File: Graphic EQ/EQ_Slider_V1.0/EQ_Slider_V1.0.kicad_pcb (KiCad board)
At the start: 2 copper layers, 101.6 x 63.5 mm, 27 parts

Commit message: small updates
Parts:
- moved TP1 3.23 mm to (195.8, 85.0)
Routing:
- net Net-(RV1-Pad3): track 148.7 -> 151.9 mm
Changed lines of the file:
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@@
 			(psa4output no)
 			(plot_black_and_white yes)
-			(plotinvisibletext no)
 			(sketchpadsonfab no)
 			(plotpadnumbers no)
@@
 	(footprint "HiroFootprints:Out_Hole_3.4_1.8"
 		(layer "F.Cu")
-		(at 195.8 88.23)
+		(at 195.8 85)
 		(property "Reference" "TP1"
 			(at 0 -0.5 0)
@@
 		)
 		(property "Value" "Cut (L)"
-			(at 0 -2.855875 0)
+			(at 0 3 0)
 			(unlocked yes)
 			(layer "F.SilkS")
@@
 	)
 	(segment
-		(start 195.8 88.23)
-		(end 195.8 122.39)
-		(width 1.6)
-		(layer "F.Cu")
-		(net 15)
-	)
-	(segment
 		(start 142.02 124.77)
 		(end 144 126.75)
@@
 		(width 1.6)
 		(layer "F.Cu")
+		(net 15)
+	)
+	(segment
+		(start 195.8 122.39)
+		(end 195.8 85)
+		(width 1.6)
+		(layer "F.Cu")

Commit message: Made slider board more compact
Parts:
- moved TP1 19.8 mm to (195.9, 104.8)
- moved TP3 19.8 mm to (195.9, 90.7)
- moved TP2 19.8 mm to (195.9, 98.1)
- moved REF** 6.27 mm to (196.6, 126.4)
- moved REF** 6.27 mm to (196.6, 71.5)
- moved REF** 0.40 mm to (109.9, 126.4)
- moved REF** 0.39 mm to (109.9, 71.5)
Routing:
- net Net-(RV1-Pad3): track 151.9 -> 128.0 mm
- net Net-(RV1-Pad1): track 69.2 -> 84.6 mm
- net Net-(C1-Pad1): track 92.2 -> 106.9 mm
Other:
- board size 101.6 x 63.5 mm -> 95.3 x 63.5 mm
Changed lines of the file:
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@@
 	(footprint "MountingHole:MountingHole_4mm"
 		(layer "F.Cu")
-		(at 202.82 126.03)
+		(at 196.56 126.43)
 		(descr "Mounting Hole 4mm, no annular")
 		(tags "mounting hole 4mm no annular")
@@
 	(footprint "HiroFootprints:Out_Hole_3.4_1.8"
 		(layer "F.Cu")
-		(at 195.8 85)
+		(at 195.88 104.84)
 		(property "Reference" "TP1"
 			(at 0 -0.5 0)
@@
 	(footprint "MountingHole:MountingHole_4mm"
 		(layer "F.Cu")
-		(at 109.82 71.15)
+		(at 109.88 71.54)
 		(descr "Mounting Hole 4mm, no annular")
 		(tags "mounting hole 4mm no annular")
@@
 	(footprint "HiroFootprints:Out_Hole_3.4_1.8"
 		(layer "F.Cu")
-		(at 195.8 70.83)
+		(at 195.88 90.67)
 		(property "Reference" "TP3"
 			(at 0 -0.5 0)
@@
 	(footprint "MountingHole:MountingHole_4mm"
 		(layer "F.Cu")
-		(at 202.82 71.15)
+		(at 196.56 71.54)
 		(descr "Mounting Hole 4mm, no annular")
 		(tags "mounting hole 4mm no annular")
@@
 	(footprint "MountingHole:MountingHole_4mm"
 		(layer "F.Cu")
-		(at 109.82 126.03)
+		(at 109.88 126.43)
 		(descr "Mounting Hole 4mm, no annular")
 		(tags "mounting hole 4mm no annular")
@@
 	(footprint "HiroFootprints:Out_Hole_3.4_1.8"
 		(layer "F.Cu")
-		(at 195.8 78.23)
+		(at 195.88 98.07)
 		(property "Reference" "TP2"
 			(at 0 -0.5 0)
@@
 	)
 	(gr_rect
-		(start 105.52 66.84)
-		(end 207.12 130.34)
+		(start 105.58 67.24)
+		(end 200.83 130.74)
 		(stroke
 			(width 0.05)
@@
 	)
 	(gr_text "Ver 1.0"
-		(at 186.31 101.29 0)
+		(at 184.88 101.36 0)
 		(layer "F.SilkS")
 		(effects
@@
 	)
 	(gr_text "HCF\nEQ Slider"
-		(at 188.62 98.85 0)
+		(at 187.19 98.92 0)
 		(layer "F.SilkS")
 		(effects
@@
 	)
 	(segment
-		(start 195.79 70.82)
-		(end 195.8 70.83)
+		(start 136.33 70.81)
+		(end 147.0975 70.81)
 		(width 1.6)
 		(layer "F.Cu")
@@
 	)
 	(segment
-		(start 136.33 70.81)
-		(end 147.0975 70.81)
+		(start 195.88 79.75)
+		(end 195.88 90.67)
+		(width 1.6)
+		(layer "F.Cu")
+		(net 1)
+	)
+	(segment
+		(start 186.95 70.82)
+		(end 195.88 79.75)
 		(width 1.6)
 		(layer "F.Cu")
@@
 	)
 	(segment
-		(start 147.0975 70.81)
-		(end 162.4475 70.81)
+		(start 177.5875 70.82)
+		(end 186.95 70.82)
 		(width 1.6)
 		(layer "F.Cu")
@@
 	)
 	(segment
-		(start 115.46 82.22)
-		(end 126.87 70.81)
+		(start 147.0975 70.81)
+		(end 162.4475 70.81)
 		(width 1.6)
 		(layer "F.Cu")
@@
 	)
 	(segment
-		(start 177.5875 70.82)
-		(end 195.79 70.82)
+		(start 115.46 82.22)
+		(end 126.87 70.81)
 		(width 1.6)
 		(layer "F.Cu")
@@
 	(segment
 		(start 188.18 118.495)
-		(end 188.18 124.68)
+		(end 188.18 125.88)
 		(width 1.6)
 		(layer "F.Cu")
@@
 	)
 	(segment
-		(start 191.44 126.75)
-		(end 190.25 126.75)
-		(width 1.6)
-		(layer "F.Cu")
-		(net 15)
-	)
-	(segment
-		(start 182.5 126.75)
-		(end 190.25 126.75)
+		(start 126.64 124.89)
+		(end 126.75 125)
 		(width 1.6)
 		(layer "F.Cu")
@@
 	)
 	(segment
-		(start 126.64 124.89)
-		(end 126.75 125)
+		(start 157.41 124.66)
+		(end 159.5 126.75)
 		(width 1.6)
 		(layer "F.Cu")
@@
 	)
 	(segment
-		(start 195.8 122.39)
-		(end 191.44 126.75)
+		(start 157.41 118.495)
+		(end 157.41 124.66)
 		(width 1.6)
 		(layer "F.Cu")
@@
 	)
 	(segment
-		(start 157.41 124.66)
-		(end 159.5 126.75)
+		(start 188.18 125.88)
+		(end 188.185 125.885)
 		(width 1.6)
 		(layer "F.Cu")
@@
 	)
 	(segment
-		(start 157.41 118.495)
-		(end 157.41 124.66)
+		(start 142.02 124.77)
+		(end 144 126.75)
 		(width 1.6)
 		(layer "F.Cu")
@@
 	)
 	(segment
-		(start 142.02 124.77)
-		(end 144 126.75)
+		(start 174.75 126.75)
+		(end 187.32 126.75)
 		(width 1.6)
 		(layer "F.Cu")
@@
 	)
 	(segment
-		(start 188.18 124.68)
-		(end 190.25 126.75)
+		(start 187.32 126.75)
+		(end 188.185 125.885)
 		(width 1.6)
 		(layer "F.Cu")
@@
 	)
 	(segment
-		(start 174.75 126.75)
-		(end 182.5 126.75)
+		(start 142.02 118.495)
+		(end 142.02 124.77)
 		(width 1.6)
 		(layer "F.Cu")
@@
 	)
 	(segment
-		(start 142.02 118.495)
-		(end 142.02 124.77)
+		(start 195.88 118.19)
+		(end 195.88 104.84)
 		(width 1.6)
 		(layer "F.Cu")
@@
 	)
 	(segment
-		(start 195.8 122.39)
-		(end 195.8 85)
+		(start 159.5 126.75)
+		(end 174.75 126.75)
 		(width 1.6)
 		(layer "F.Cu")
@@
 	)
 	(segment
-		(start 159.5 126.75)
-		(end 174.75 126.75)
+		(start 188.185 125.885)
+		(end 195.88 118.19)
 		(width 1.6)
 		(layer "F.Cu")
@@
 	)
 	(segment
-		(start 195.785 78.215)
-		(end 195.8 78.23)
+		(start 172.79 78.215)
+		(end 188.18 78.215)
 		(width 1.6)
 		(layer "F.Cu")
@@
 	)
 	(segment
-		(start 172.79 78.215)
-		(end 188.18 78.215)
+		(start 126.64 78.215)
+		(end 142.02 78.215)
 		(width 1.6)
 		(layer "F.Cu")
@@
 	)
 	(segment
-		(start 126.64 78.215)
-		(end 142.02 78.215)
+		(start 188.18 90.37)
+		(end 195.88 98.07)
 		(width 1.6)
 		(layer "F.Cu")
@@
 	(segment
 		(start 188.18 78.215)
-		(end 195.785 78.215)
+		(end 188.18 90.37)
 		(width 1.6)
 		(layer "F.Cu")
@@
 		)
 	)
+	(group ""
+		(members "0c7bc8e3-a588-43e6-956f-7a970030289d" "d775e616-bb41-4192-8a43-31805b470f2c")
+	)
 	(embedded_fonts no)

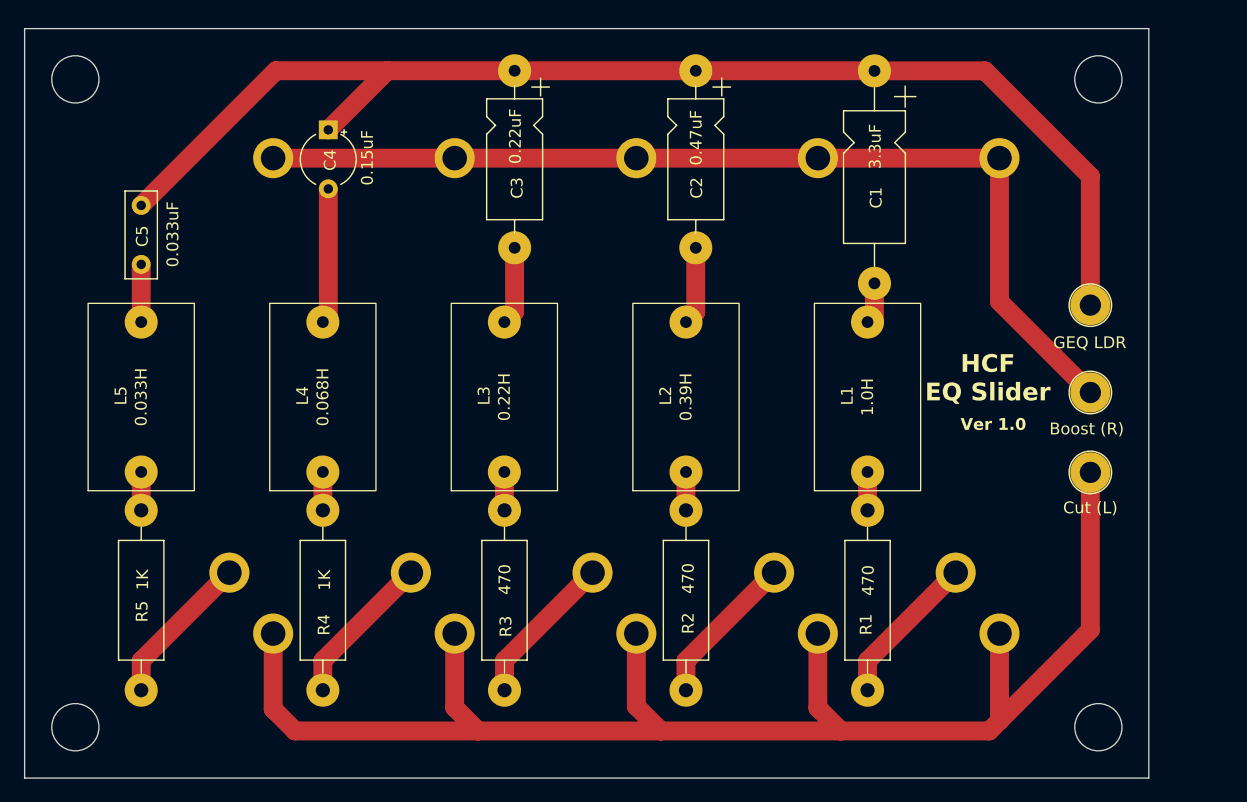
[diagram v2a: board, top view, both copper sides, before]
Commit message: increased trace width
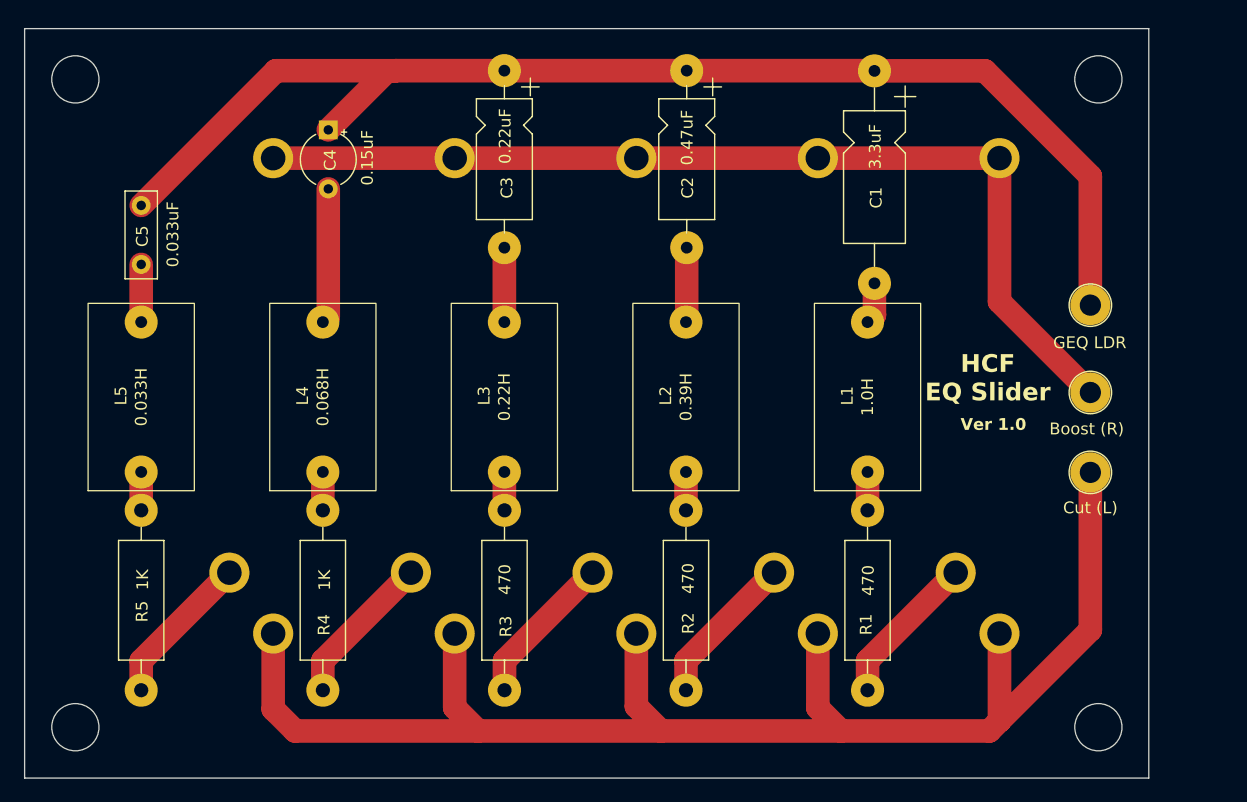
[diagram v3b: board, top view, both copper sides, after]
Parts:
- moved C3 0.87 mm to (146.2, 70.8)
- moved C2 0.77 mm to (161.7, 70.8)
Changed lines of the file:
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@@
 	(footprint "Capacitor_THT:CP_Axial_L10.0mm_D4.5mm_P15.00mm_Horizontal"
 		(layer "F.Cu")
-		(at 162.4475 70.81 -90)
+		(at 161.68 70.8 -90)
 		(descr "CP, Axial series, Axial, Horizontal, pin pitch=15mm, , length*diameter=10*4.5mm^2, Electrolytic Capacitor, , http://www.vishay.com/docs/28325/021asm.pdf")
 		(tags "CP Axial series Axial Horizontal pin pitch 15mm  length 10mm diameter 4.5mm Electrolytic Capacitor")
@@
 	(footprint "Capacitor_THT:CP_Axial_L10.0mm_D4.5mm_P15.00mm_Horizontal"
 		(layer "F.Cu")
-		(at 147.0975 70.81 -90)
+		(at 146.23 70.8 -90)
 		(descr "CP, Axial series, Axial, Horizontal, pin pitch=15mm, , length*diameter=10*4.5mm^2, Electrolytic Capacitor, , http://www.vishay.com/docs/28325/021asm.pdf")
 		(tags "CP Axial series Axial Horizontal pin pitch 15mm  length 10mm diameter 4.5mm Electrolytic Capacitor")
@@
 	)
 	(segment
-		(start 162.4475 70.81)
-		(end 177.5775 70.81)
-		(width 1.6)
-		(layer "F.Cu")
-		(net 1)
-	)
-	(segment
-		(start 136.33 70.81)
-		(end 147.0975 70.81)
-		(width 1.6)
-		(layer "F.Cu")
-		(net 1)
-	)
-	(segment
 		(start 195.88 79.75)
 		(end 195.88 90.67)
-		(width 1.6)
+		(width 2)
 		(layer "F.Cu")
 		(net 1)
@@
 		(start 186.95 70.82)
 		(end 195.88 79.75)
-		(width 1.6)
+		(width 2)
+		(layer "F.Cu")
+		(net 1)
+	)
+	(segment
+		(start 146.23 70.8)
+		(end 161.68 70.8)
+		(width 2)
 		(layer "F.Cu")
 		(net 1)
@@
 		(start 131.31 75.82)
 		(end 136.32 70.81)
-		(width 1.6)
+		(width 2)
 		(layer "F.Cu")
 		(net 1)
@@
 		(start 177.5875 70.82)
 		(end 186.95 70.82)
-		(width 1.6)
+		(width 2)
 		(layer "F.Cu")
 		(net 1)
 	)
 	(segment
-		(start 147.0975 70.81)
-		(end 162.4475 70.81)
-		(width 1.6)
+		(start 161.68 70.8)
+		(end 177.5675 70.8)
+		(width 2)
+		(layer "F.Cu")
+		(net 1)
+	)
+	(segment
+		(start 136.99 70.81)
+		(end 137 70.8)
+		(width 2)
 		(layer "F.Cu")
 		(net 1)
@@
 		(start 115.46 82.22)
 		(end 126.87 70.81)
-		(width 1.6)
+		(width 2)
 		(layer "F.Cu")
 		(net 1)
 	)
 	(segment
-		(start 136.32 70.81)
-		(end 136.33 70.81)
-		(width 1.6)
+		(start 136.33 70.81)
+		(end 136.99 70.81)
+		(width 2)
 		(layer "F.Cu")
 		(net 1)
 	)
 	(segment
-		(start 177.5775 70.81)
+		(start 177.5675 70.8)
 		(end 177.5875 70.82)
-		(width 1.6)
+		(width 2)
+		(layer "F.Cu")
+		(net 1)
+	)
+	(segment
+		(start 137 70.8)
+		(end 146.23 70.8)
+		(width 2)
+		(layer "F.Cu")
+		(net 1)
+	)
+	(segment
+		(start 136.32 70.81)
+		(end 136.33 70.81)
+		(width 2)
 		(layer "F.Cu")
 		(net 1)
@@
 		(start 126.87 70.81)
 		(end 136.33 70.81)
-		(width 1.6)
+		(width 2)
 		(layer "F.Cu")
 		(net 1)
@@
 		(start 177.5875 88.82)
 		(end 177.5875 91.5175)
-		(width 1.6)
+		(width 2)
 		(layer "F.Cu")
 		(net 2)
@@
 		(start 177.5875 91.5175)
 		(end 177 92.105)
-		(width 1.6)
+		(width 2)
 		(layer "F.Cu")
 		(net 2)
 	)
 	(segment
-		(start 162.4475 85.81)
-		(end 162.4475 91.275)
-		(width 1.6)
+		(start 161.68 92.0425)
+		(end 161.6175 92.105)
+		(width 2)
 		(layer "F.Cu")
 		(net 3)
 	)
 	(segment
-		(start 162.4475 91.275)
-		(end 161.6175 92.105)
-		(width 1.6)
+		(start 161.68 85.8)
+		(end 161.68 92.0425)
+		(width 2)
 		(layer "F.Cu")
 		(net 3)
 	)
 	(segment
-		(start 147.0975 91.2375)
+		(start 146.23 85.8)
 		(end 146.23 92.105)
-		(width 1.6)
-		(layer "F.Cu")
-		(net 4)
-	)
-	(segment
-		(start 147.0975 85.81)
-		(end 147.0975 91.2375)
-		(width 1.6)
+		(width 2)
 		(layer "F.Cu")
 		(net 4)
@@
 		(start 177 123.295)
 		(end 177 120.805)
-		(width 1.6)
+		(width 2)
 		(layer "F.Cu")
 		(net 5)
@@
 		(start 177 120.805)
 		(end 184.47 113.335)
-		(width 1.6)
+		(width 2)
 		(layer "F.Cu")
 		(net 5)
@@
 		(start 177 104.805)
 		(end 177 108.055)
-		(width 1.6)
+		(width 2)
 		(layer "F.Cu")
 		(net 6)
@@
 		(start 161.6175 104.805)
 		(end 161.6175 108.055)
-		(width 1.6)
+		(width 2)
 		(layer "F.Cu")
 		(net 7)
@@
 		(start 161.6175 120.7975)
 		(end 169.08 113.335)
-		(width 1.6)
+		(width 2)
 		(layer "F.Cu")
 		(net 8)
@@
 		(start 161.6175 123.295)
 		(end 161.6175 120.7975)
-		(width 1.6)
+		(width 2)
 		(layer "F.Cu")
 		(net 8)
@@
 		(start 146.24 120.795)
 		(end 153.7 113.335)
-		(width 1.6)
+		(width 2)
 		(layer "F.Cu")
 		(net 9)
@@
 		(start 146.24 123.295)
 		(end 146.24 120.795)
-		(width 1.6)
+		(width 2)
 		(layer "F.Cu")
 		(net 9)
@@
 		(start 146.23 108.045)
 		(end 146.24 108.055)
-		(width 1.6)
+		(width 2)
 		(layer "F.Cu")
 		(net 10)
@@
 		(start 146.23 104.805)
 		(end 146.23 108.045)
-		(width 1.6)
+		(width 2)
 		(layer "F.Cu")
 		(net 10)
@@
 		(start 130.85 123.295)
 		(end 130.85 120.795)
-		(width 1.6)
+		(width 2)
 		(layer "F.Cu")
 		(net 11)
@@
 		(start 130.85 120.795)
 		(end 138.31 113.335)
-		(width 1.6)
+		(width 2)
 		(layer "F.Cu")
 		(net 11)
@@
 		(start 130.85 104.805)
 		(end 130.85 108.055)
-		(width 1.6)
+		(width 2)
 		(layer "F.Cu")
 		(net 12)
@@
 		(start 115.46 104.805)
 		(end 115.46 108.055)
-		(width 1.6)
+		(width 2)
 		(layer "F.Cu")
 		(net 13)
@@
 		(start 115.46 123.295)
 		(end 115.46 120.805)
-		(width 1.6)
+		(width 2)
 		(layer "F.Cu")
 		(net 14)
@@
 		(start 115.46 120.805)
 		(end 122.93 113.335)
-		(width 1.6)
+		(width 2)
 		(layer "F.Cu")
 		(net 14)
@@
 		(start 188.18 118.495)
 		(end 188.18 125.88)
-		(width 1.6)
+		(width 2)
 		(layer "F.Cu")
 		(net 15)
@@
 		(start 126.64 124.89)
 		(end 126.75 125)
-		(width 1.6)
+		(width 2)
 		(layer "F.Cu")
 		(net 15)
@@
 		(start 157.41 124.66)
 		(end 159.5 126.75)
-		(width 1.6)
+		(width 2)
 		(layer "F.Cu")
 		(net 15)
@@
 		(start 157.41 118.495)
 		(end 157.41 124.66)
-		(width 1.6)
+		(width 2)
 		(layer "F.Cu")
 		(net 15)
@@
 		(start 188.18 125.88)
 		(end 188.185 125.885)
-		(width 1.6)
+		(width 2)
 		(layer "F.Cu")
 		(net 15)
@@
 		(start 142.02 124.77)
 		(end 144 126.75)
-		(width 1.6)
+		(width 2)
 		(layer "F.Cu")
 		(net 15)
@@
 		(start 174.75 126.75)
 		(end 187.32 126.75)
-		(width 1.6)
+		(width 2)
 		(layer "F.Cu")
 		(net 15)
@@
 		(start 126.75 125)
 		(end 128.5 126.75)
-		(width 1.6)
+		(width 2)
 		(layer "F.Cu")
 		(net 15)
@@
 		(start 172.79 118.495)
 		(end 172.79 124.79)
-		(width 1.6)
+		(width 2)
 		(layer "F.Cu")
 		(net 15)
@@
 		(start 187.32 126.75)
 		(end 188.185 125.885)
-		(width 1.6)
+		(width 2)
 		(layer "F.Cu")
 		(net 15)
@@
 		(start 144 126.75)
 		(end 159.5 126.75)
-		(width 1.6)
+		(width 2)
 		(layer "F.Cu")
 		(net 15)
@@
 		(start 126.64 118.495)
 		(end 126.64 124.89)
-		(width 1.6)
+		(width 2)
 		(layer "F.Cu")
 		(net 15)
@@
 		(start 142.02 118.495)
 		(end 142.02 124.77)
-		(width 1.6)
+		(width 2)
 		(layer "F.Cu")
 		(net 15)
@@
 		(start 195.88 118.19)
 		(end 195.88 104.84)
-		(width 1.6)
+		(width 2)
 		(layer "F.Cu")
 		(net 15)
@@
 		(start 172.79 124.79)
 		(end 174.75 126.75)
-		(width 1.6)
+		(width 2)
 		(layer "F.Cu")
 		(net 15)
@@
 		(start 128.5 126.75)
 		(end 144 126.75)
-		(width 1.6)
+		(width 2)
 		(layer "F.Cu")
 		(net 15)
@@
 		(start 159.5 126.75)
 		(end 174.75 126.75)
-		(width 1.6)
+		(width 2)
 		(layer "F.Cu")
 		(net 15)
@@
 		(start 188.185 125.885)
 		(end 195.88 118.19)
-		(width 1.6)
+		(width 2)
 		(layer "F.Cu")
 		(net 15)
@@
 		(start 142.02 78.215)
 		(end 157.41 78.215)
-		(width 1.6)
+		(width 2)
 		(layer "F.Cu")
 		(net 16)
@@
 		(start 157.41 78.215)
 		(end 172.79 78.215)
-		(width 1.6)
+		(width 2)
 		(layer "F.Cu")
 		(net 16)
@@
 		(start 172.79 78.215)
 		(end 188.18 78.215)
-		(width 1.6)
+		(width 2)
 		(layer "F.Cu")
 		(net 16)
@@
 		(start 126.64 78.215)
 		(end 142.02 78.215)
-		(width 1.6)
+		(width 2)
 		(layer "F.Cu")
 		(net 16)
@@
 		(start 188.18 90.37)
 		(end 195.88 98.07)
-		(width 1.6)
+		(width 2)
 		(layer "F.Cu")
 		(net 16)
@@
 		(start 188.18 78.215)
 		(end 188.18 90.37)
-		(width 1.6)
+		(width 2)
 		(layer "F.Cu")
 		(net 16)
@@
 		(start 115.46 92.105)
 		(end 115.46 87.22)
-		(width 1.6)
+		(width 2)
 		(layer "F.Cu")
 		(net 17)
@@
 		(start 131.31 91.645)
 		(end 130.85 92.105)
-		(width 1.6)
+		(width 2)
 		(layer "F.Cu")
 		(net 18)
@@
 		(start 131.31 80.82)
 		(end 131.31 91.645)
-		(width 1.6)
+		(width 2)
 		(layer "F.Cu")
 		(net 18)

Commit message: Adjusted Resistor Sizes
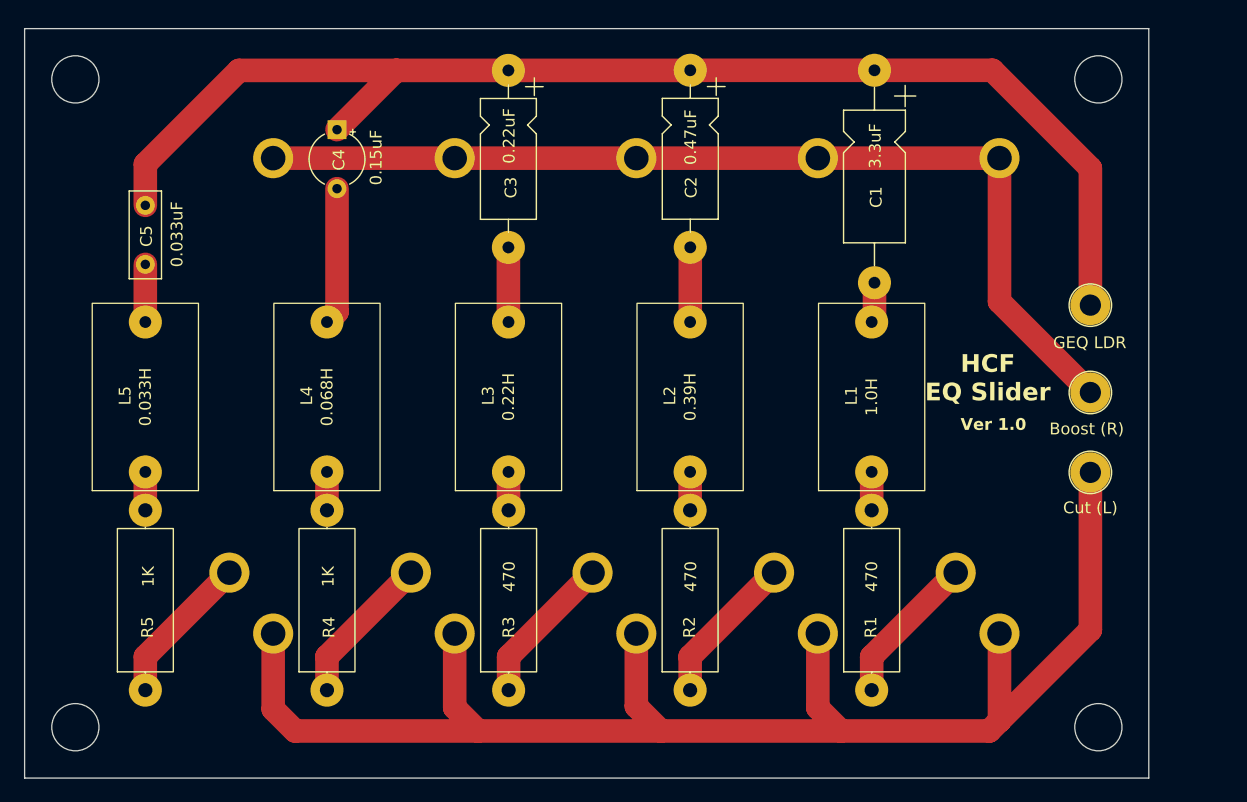
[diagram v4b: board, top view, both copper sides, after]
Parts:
- R1, R2, R3, R4, R5: footprint Resistor_THT:R_Axial_DIN0411_L9.9mm_D3.6mm_P15.24mm_Horizontal -> Resistor_THT:R_Axial_DIN0414_L11.9mm_D4.5mm_P15.24mm_Horizontal
- moved C4 0.74 mm to (132.1, 75.8)
- moved L3 0.35 mm to (146.6, 104.8)
- moved L5 0.35 mm to (115.8, 104.8)
- moved C5 0.35 mm to (115.8, 82.2)
- moved R5 0.35 mm to (115.8, 123.3)
- moved L1 0.35 mm to (177.3, 104.8)
- moved L2 0.35 mm to (162.0, 104.8)
- moved L4 0.35 mm to (131.2, 104.8)
- moved R1 0.35 mm to (177.3, 123.3)
- moved R2 0.35 mm to (162.0, 123.3)
- moved R3 0.35 mm to (146.6, 123.3)
- moved R4 0.35 mm to (131.2, 123.3)
- moved C3 0.34 mm to (146.6, 70.8)
- moved C2 0.30 mm to (162.0, 70.8)
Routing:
- net Net-(C1-Pad1): track 106.9 -> 109.0 mm

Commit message: Preamp Progress, and Custom Footprint Library
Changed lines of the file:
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@@
-	)
-	(segment
-		(start 146.23 108.045)
-		(end 146.24 108.055)
-		(width 2)
-		(layer "F.Cu")
-		(net 10)
 	)
 	(segment
@@
 	)
 	(segment
-		(start 126.64 124.89)
-		(end 126.75 125)
-		(width 2)
-		(layer "F.Cu")
-		(net 15)
-	)
-	(segment
 		(start 157.41 124.66)
 		(end 159.5 126.75)
@@
 	)
 	(segment
-		(start 126.75 125)
+		(start 126.64 124.89)
 		(end 128.5 126.75)
 		(width 2)
